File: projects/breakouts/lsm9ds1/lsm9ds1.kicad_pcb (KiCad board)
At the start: 2 copper layers, 17.8 x 12.7 mm, 7 parts, among them P1 CONN_01X04, U1 LSM9DS1

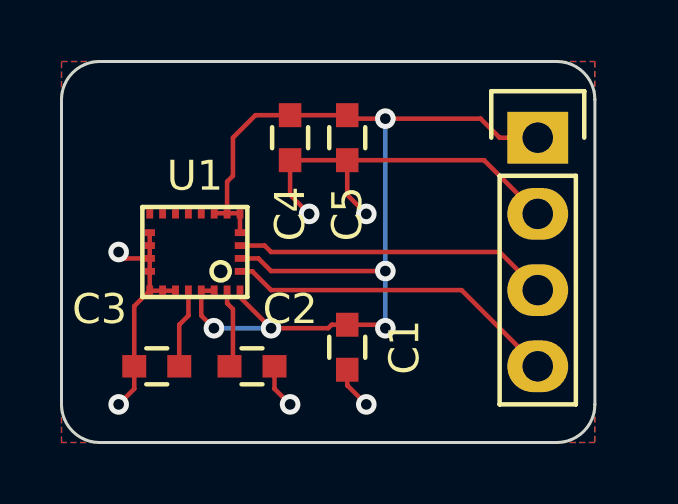
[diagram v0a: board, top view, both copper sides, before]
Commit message: Minor tweaks on gyro/accel/mag breakout; updated old tssop/soic breakout to tssop28 which fits in 500mil.
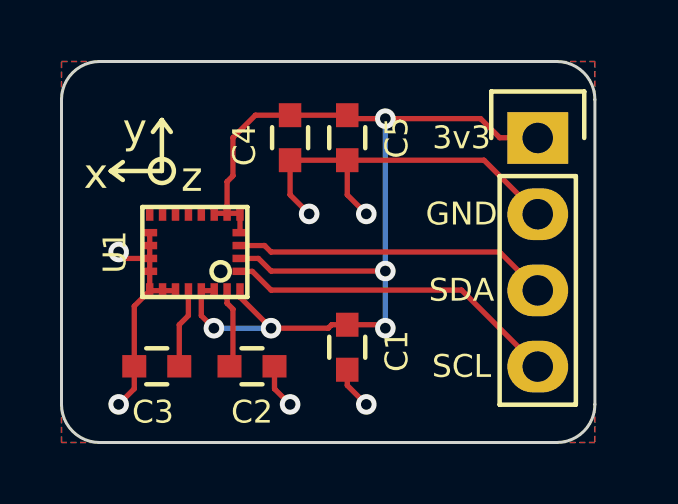
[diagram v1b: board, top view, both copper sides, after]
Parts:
- U1: footprint Digital Cave:LGA-24L -> LGA-24L
- moved P1 3.81 mm to (160.7, 106.7)
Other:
- net class Default: clearance 0.1524 -> 0.1778; trace_width 0.1524 -> 0.1778
- rule trace_clearance: 0.1524 -> 0.1778
- rule trace_min: 0.1524 -> 0.1778
- board text added: "U1: LSM9DS1 C1: 100nF C2: 100nF C3: 10nF C4: 100nF C5: 10uF"

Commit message: Reduced lsm9ds1 breakout to 0.4" square
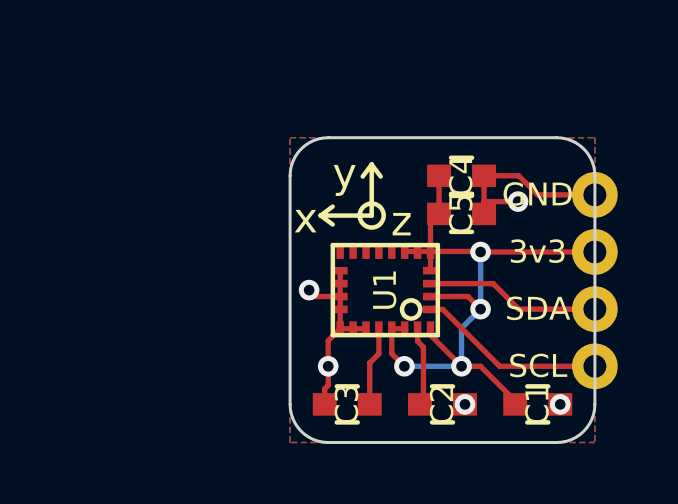
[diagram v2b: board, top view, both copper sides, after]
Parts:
- moved C1 6.63 mm to (160.7, 111.8), turned to 0 degrees
- moved C2 6.48 mm to (157.5, 111.8)
- moved C3 6.48 mm to (154.3, 111.8)
- moved U1 6.48 mm to (155.6, 108.0)
- moved C4 5.85 mm to (158.1, 104.1), turned to 0 degrees
- moved C5 4.58 mm to (158.1, 105.4), turned to 0 degrees
- moved P1 2.29 mm to (162.6, 108.0)
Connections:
- P1 pad 1: +3V3 -> GND
- P1 pad 2: GND -> +3V3
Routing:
- net +3V3: track 36.2 -> 23.4 mm, vias 5 -> 4
- net GND: track 24.3 -> 13.9 mm, vias 6 -> 5
- net /SCL: track 11.2 -> 6.26 mm
- net /SDA: track 10.5 -> 5.83 mm
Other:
- board size 17.8 x 12.7 mm -> 10.2 x 10.2 mm
